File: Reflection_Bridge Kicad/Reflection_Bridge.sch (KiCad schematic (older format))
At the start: 7 parts, among them P1 SMA_Female, P2 SMA_Female, P3 SMA_Female, T1 Transformer_1P_1S

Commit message: Added fix me notes to Reflection Bridge!
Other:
- note added: "T1 footprint is really badly done. Fix it before making another board!"
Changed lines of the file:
@@
 EESchema Schematic File Version 4
 LIBS:Reflection_Bridge-cache
-EELAYER 26 0
+EELAYER 29 0
 EELAYER END
 $Descr USLetter 11000 8500
@@
 Wire Wire Line
 	5150 3850 5150 4350
+Text Notes 3700 5350 0    50   ~ 0
+T1 footprint is really badly done.  Fix it before making another board!
 $EndSCHEMATC

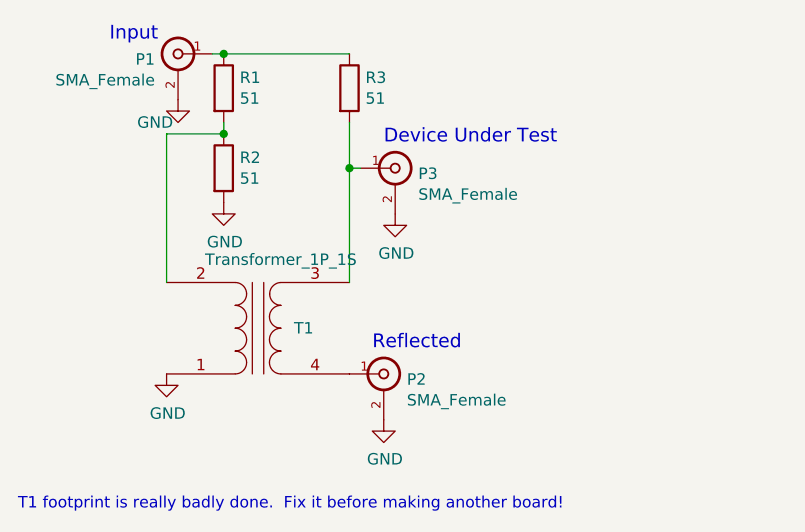
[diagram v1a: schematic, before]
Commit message: Fixed the reflection bridge, and some bugs in octave scripts.
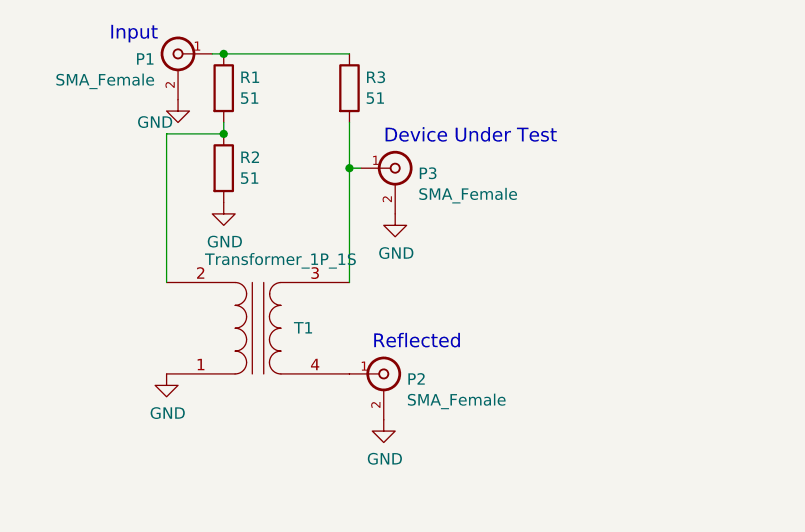
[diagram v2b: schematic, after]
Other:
- note removed: "T1 footprint is really badly done. Fix it before making another board!"
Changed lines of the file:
@@
 Sheet 1 1
 Title "Reflection Bridge"
-Date "2017-04-20"
-Rev "0.1"
+Date "2019-05-16"
+Rev "0.2"
 Comp "Walla Walla University"
 Comment1 "Rob Frohne"
@@
 Wire Wire Line
 	5150 3850 5150 4350
-Text Notes 3700 5350 0    50   ~ 0
-T1 footprint is really badly done.  Fix it before making another board!
 $EndSCHEMATC
